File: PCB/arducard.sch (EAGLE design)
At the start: 94 parts, among them J1 USB MICRO, Q1 BC817-16LT1SMD, Q2 DMG2301U-7, Q3 2N7002, Q4 BSS84, Q5 2N7002, Q6 2N7002, Q7 2N7002, Q8 BSS84, Q9 DMG2301U-7, U1 microSD, U2 ATMEGA32U4-XUAU, Y1 8MHz KX-7

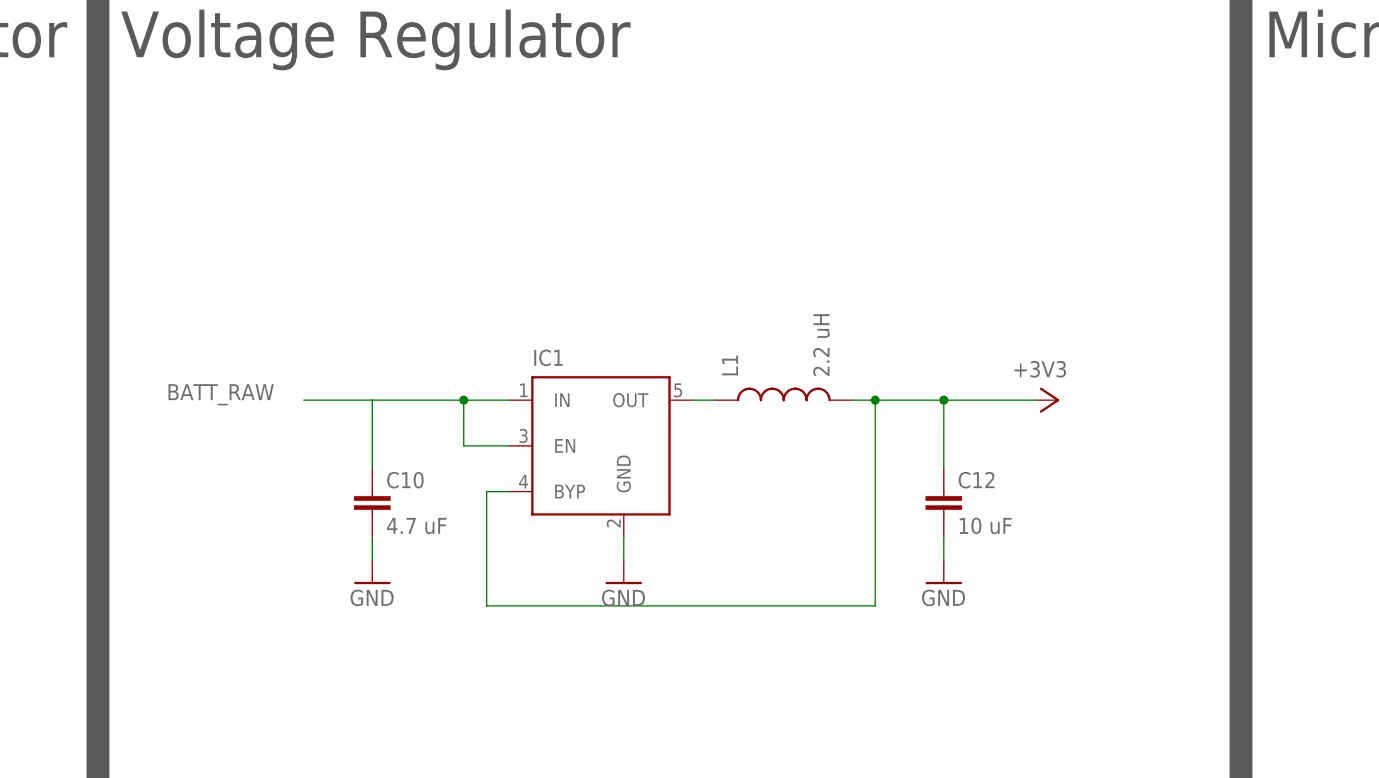
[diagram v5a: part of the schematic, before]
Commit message: added switch between Vusb and battery
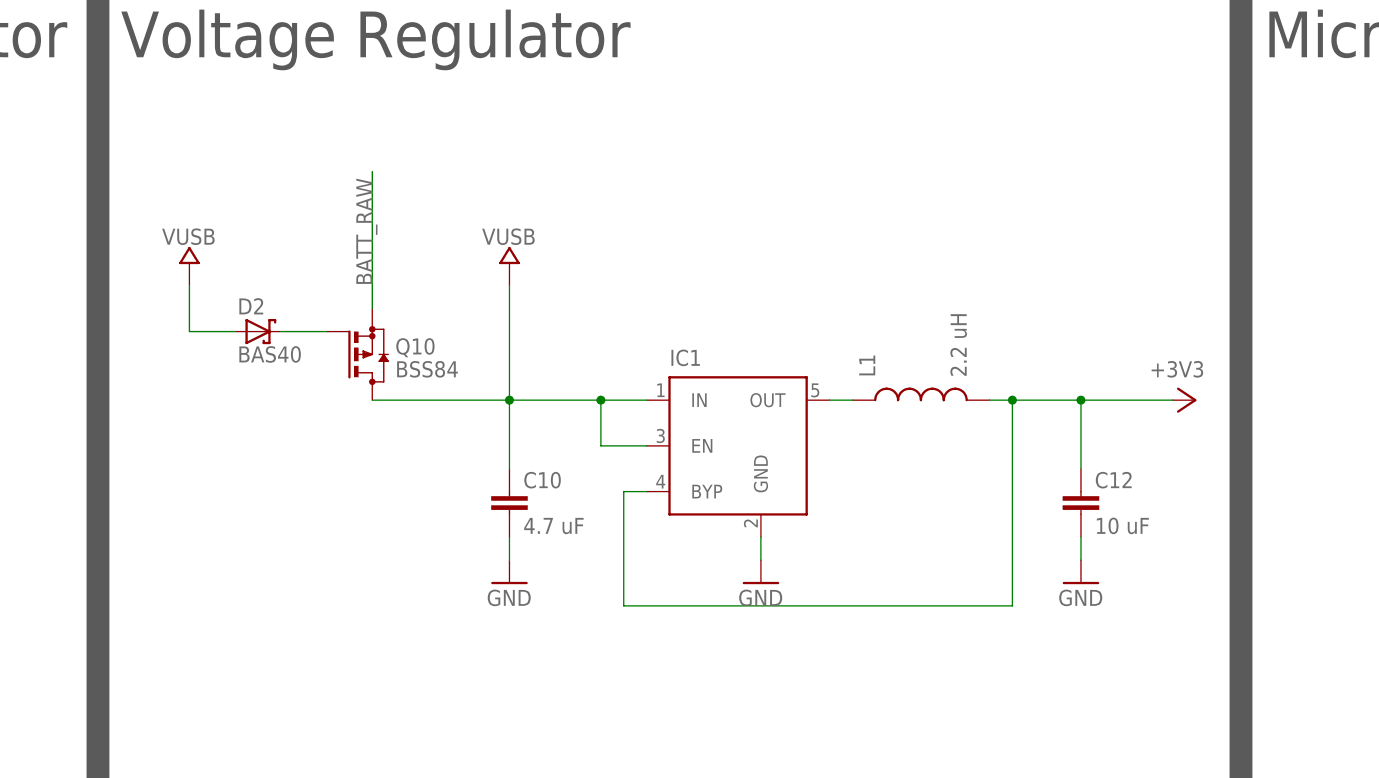
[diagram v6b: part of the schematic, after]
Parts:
- added D2: BAS40, diode:BAS40
- added Q10: BSS84, transistor-small-signal:BSS84
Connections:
- new net N$35: D2.C, Q10.G
- net BATT_RAW: now also Q10.S; no longer C10.1, IC1.EN, IC1.IN
- net VUSB: now also C10.1, D2.A, IC1.EN, IC1.IN, Q10.D
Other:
- moved on the sheet: C10, C12, IC1, L1
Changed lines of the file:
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@@
 <part name="+3V10" library="supply1" deviceset="+3V3" device=""/>
 <part name="GND31" library="supply1" deviceset="GND" device=""/>
+<part name="Q10" library="transistor-small-signal" deviceset="BSS84" device=""/>
+<part name="U$12" library="MyPOW" deviceset="VUSB" device=""/>
+<part name="D2" library="diode" deviceset="BAS40" device=""/>
+<part name="U$13" library="MyPOW" deviceset="VUSB" device=""/>
 </parts>
 <sheets>
@@
 <instance part="C5" gate="G$1" x="335.28" y="254"/>
 <instance part="+3V4" gate="G$1" x="45.72" y="142.24"/>
-<instance part="IC1" gate="G1" x="528.32" y="243.84"/>
-<instance part="L1" gate="G$1" x="548.64" y="248.92" rot="R90"/>
-<instance part="C12" gate="G$1" x="566.42" y="238.76"/>
-<instance part="+3V5" gate="G$1" x="579.12" y="248.92" rot="R270"/>
+<instance part="IC1" gate="G1" x="543.56" y="243.84"/>
+<instance part="L1" gate="G$1" x="563.88" y="248.92" rot="R90"/>
+<instance part="C12" gate="G$1" x="581.66" y="238.76"/>
+<instance part="+3V5" gate="G$1" x="594.36" y="248.92" rot="R270"/>
 <instance part="+3V6" gate="G$1" x="678.18" y="246.38" rot="R270"/>
 <instance part="U$8" gate="G$1" x="60.96" y="264.16"/>
@@
 <instance part="GND5" gate="1" x="127" y="228.6" rot="R270"/>
 <instance part="GND7" gate="1" x="642.62" y="218.44"/>
-<instance part="GND11" gate="1" x="530.86" y="228.6"/>
-<instance part="GND13" gate="1" x="566.42" y="228.6"/>
+<instance part="GND11" gate="1" x="546.1" y="228.6"/>
+<instance part="GND13" gate="1" x="581.66" y="228.6"/>
 <instance part="Q1" gate="G$1" x="406.4" y="86.36"/>
 <instance part="R15" gate="G$1" x="386.08" y="86.36" smashed="yes">
@@
 <instance part="+3V7" gate="G$1" x="299.72" y="254" rot="R270"/>
 <instance part="GND12" gate="1" x="238.76" y="223.52"/>
-<instance part="C10" gate="G$1" x="502.92" y="238.76"/>
-<instance part="GND17" gate="1" x="502.92" y="228.6"/>
+<instance part="C10" gate="G$1" x="518.16" y="238.76"/>
+<instance part="GND17" gate="1" x="518.16" y="228.6"/>
 <instance part="+3V8" gate="G$1" x="220.98" y="236.22" rot="R90"/>
 <instance part="+3V10" gate="G$1" x="241.3" y="269.24"/>
 <instance part="GND31" gate="1" x="292.1" y="233.68"/>
+<instance part="Q10" gate="G$1" x="502.92" y="254"/>
+<instance part="U$12" gate="G$1" x="518.16" y="264.16"/>
+<instance part="D2" gate="1" x="490.22" y="256.54"/>
+<instance part="U$13" gate="G$1" x="482.6" y="264.16"/>
 </instances>
 <busses>
@@
 <segment>
 <pinref part="IC1" gate="G1" pin="GND"/>
-<wire x1="530.86" y1="233.68" x2="530.86" y2="231.14" width="0.1524" layer="91"/>
+<wire x1="546.1" y1="233.68" x2="546.1" y2="231.14" width="0.1524" layer="91"/>
 <pinref part="GND11" gate="1" pin="GND"/>
 </segment>
 <segment>
 <pinref part="C12" gate="G$1" pin="2"/>
-<wire x1="566.42" y1="233.68" x2="566.42" y2="231.14" width="0.1524" layer="91"/>
+<wire x1="581.66" y1="233.68" x2="581.66" y2="231.14" width="0.1524" layer="91"/>
 <pinref part="GND13" gate="1" pin="GND"/>
 </segment>
@@
 <pinref part="GND17" gate="1" pin="GND"/>
 <pinref part="C10" gate="G$1" pin="2"/>
-<wire x1="502.92" y1="231.14" x2="502.92" y2="233.68" width="0.1524" layer="91"/>
+<wire x1="518.16" y1="231.14" x2="518.16" y2="233.68" width="0.1524" layer="91"/>
 </segment>
 <segment>
@@
 <junction x="335.28" y="256.54"/>
 <label x="325.12" y="256.54" size="1.778" layer="95"/>
+</segment>
+<segment>
+<pinref part="IC1" gate="G1" pin="IN"/>
+<wire x1="528.32" y1="248.92" x2="533.4" y2="248.92" width="0.1524" layer="91"/>
+<pinref part="IC1" gate="G1" pin="EN"/>
+<wire x1="533.4" y1="243.84" x2="528.32" y2="243.84" width="0.1524" layer="91"/>
+<wire x1="528.32" y1="243.84" x2="528.32" y2="248.92" width="0.1524" layer="91"/>
+<wire x1="528.32" y1="248.92" x2="518.16" y2="248.92" width="0.1524" layer="91"/>
+<junction x="528.32" y="248.92"/>
+<pinref part="C10" gate="G$1" pin="1"/>
+<wire x1="518.16" y1="241.3" x2="518.16" y2="248.92" width="0.1524" layer="91"/>
+<pinref part="Q10" gate="G$1" pin="D"/>
+<wire x1="502.92" y1="248.92" x2="518.16" y2="248.92" width="0.1524" layer="91"/>
+<junction x="518.16" y="248.92"/>
+<pinref part="U$12" gate="G$1" pin="VUSB"/>
+<wire x1="518.16" y1="248.92" x2="518.16" y2="261.62" width="0.1524" layer="91"/>
+</segment>
+<segment>
+<pinref part="U$13" gate="G$1" pin="VUSB"/>
+<wire x1="482.6" y1="261.62" x2="482.6" y2="256.54" width="0.1524" layer="91"/>
+<pinref part="D2" gate="1" pin="A"/>
+<wire x1="482.6" y1="256.54" x2="487.68" y2="256.54" width="0.1524" layer="91"/>
 </segment>
 </net>
@@
 </segment>
 <segment>
-<wire x1="556.26" y1="248.92" x2="558.8" y2="248.92" width="0.1524" layer="91"/>
+<wire x1="571.5" y1="248.92" x2="574.04" y2="248.92" width="0.1524" layer="91"/>
 <pinref part="L1" gate="G$1" pin="2"/>
 <pinref part="C12" gate="G$1" pin="1"/>
-<wire x1="558.8" y1="248.92" x2="566.42" y2="248.92" width="0.1524" layer="91"/>
-<wire x1="566.42" y1="248.92" x2="576.58" y2="248.92" width="0.1524" layer="91"/>
-<wire x1="566.42" y1="241.3" x2="566.42" y2="248.92" width="0.1524" layer="91"/>
-<junction x="566.42" y="248.92"/>
+<wire x1="574.04" y1="248.92" x2="581.66" y2="248.92" width="0.1524" layer="91"/>
+<wire x1="581.66" y1="248.92" x2="591.82" y2="248.92" width="0.1524" layer="91"/>
+<wire x1="581.66" y1="241.3" x2="581.66" y2="248.92" width="0.1524" layer="91"/>
+<junction x="581.66" y="248.92"/>
 <pinref part="+3V5" gate="G$1" pin="+3V3"/>
 <pinref part="IC1" gate="G1" pin="BYP"/>
-<wire x1="518.16" y1="238.76" x2="515.62" y2="238.76" width="0.1524" layer="91"/>
-<wire x1="515.62" y1="238.76" x2="515.62" y2="226.06" width="0.1524" layer="91"/>
-<wire x1="515.62" y1="226.06" x2="558.8" y2="226.06" width="0.1524" layer="91"/>
-<wire x1="558.8" y1="226.06" x2="558.8" y2="248.92" width="0.1524" layer="91"/>
-<junction x="558.8" y="248.92"/>
+<wire x1="533.4" y1="238.76" x2="530.86" y2="238.76" width="0.1524" layer="91"/>
+<wire x1="530.86" y1="238.76" x2="530.86" y2="226.06" width="0.1524" layer="91"/>
+<wire x1="530.86" y1="226.06" x2="574.04" y2="226.06" width="0.1524" layer="91"/>
+<wire x1="574.04" y1="226.06" x2="574.04" y2="248.92" width="0.1524" layer="91"/>
+<junction x="574.04" y="248.92"/>
 </segment>
 <segment>
@@
 <net name="BATT_RAW" class="0">
 <segment>
-<pinref part="IC1" gate="G1" pin="IN"/>
-<wire x1="513.08" y1="248.92" x2="518.16" y2="248.92" width="0.1524" layer="91"/>
-<pinref part="IC1" gate="G1" pin="EN"/>
-<wire x1="518.16" y1="243.84" x2="513.08" y2="243.84" width="0.1524" layer="91"/>
-<wire x1="513.08" y1="243.84" x2="513.08" y2="248.92" width="0.1524" layer="91"/>
-<wire x1="513.08" y1="248.92" x2="502.92" y2="248.92" width="0.1524" layer="91"/>
-<label x="480.06" y="248.92" size="1.778" layer="95"/>
-<junction x="513.08" y="248.92"/>
-<pinref part="C10" gate="G$1" pin="1"/>
-<wire x1="502.92" y1="248.92" x2="495.3" y2="248.92" width="0.1524" layer="91"/>
-<wire x1="502.92" y1="241.3" x2="502.92" y2="248.92" width="0.1524" layer="91"/>
-</segment>
-<segment>
 <pinref part="R16" gate="G$1" pin="2"/>
 <wire x1="408.94" y1="109.22" x2="419.1" y2="109.22" width="0.1524" layer="91"/>
@@
 <pinref part="U$6" gate="G$1" pin="+"/>
 </segment>
+<segment>
+<pinref part="Q10" gate="G$1" pin="S"/>
+<wire x1="502.92" y1="259.08" x2="502.92" y2="274.32" width="0.1524" layer="91"/>
+<label x="502.92" y="261.62" size="1.778" layer="95" rot="R90"/>
+</segment>
 </net>
 <net name="N$7" class="0">
@@
 <pinref part="IC1" gate="G1" pin="OUT"/>
 <pinref part="L1" gate="G$1" pin="1"/>
-<wire x1="538.48" y1="248.92" x2="541.02" y2="248.92" width="0.1524" layer="91"/>
+<wire x1="553.72" y1="248.92" x2="556.26" y2="248.92" width="0.1524" layer="91"/>
 </segment>
 </net>
@@
 </segment>
 </net>
+<net name="N$35" class="0">
+<segment>
+<pinref part="D2" gate="1" pin="C"/>
+<pinref part="Q10" gate="G$1" pin="G"/>
+<wire x1="492.76" y1="256.54" x2="497.84" y2="256.54" width="0.1524" layer="91"/>
+</segment>
+</net>

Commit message: fixed up libraries
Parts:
- removed IC1: (no value), v-reg-micrel:MIC5219XX
- added J2: microSD, SparkFun:USD-SOCKETSMD
- C11: value 1uF -> 10 uF
- C12: value 10 uF -> 100pF
- C13: value 100pF -> 22 pF
- C14: value 22 pF -> 1uF
- C6: value 100nF -> 1uF
- C7: value 1uF -> 100nF
- D1: value BAT54S -> BAS40; device diode:BAT54S -> diode:BAS40
- D2: value BAS40 -> BAT54S; device diode:BAS40 -> diode:BAT54S
- L1: value 2.2 uH -> MH2029-300Y; device SparkFun-Passives:INDUCTOR30OHM,1.8A -> wuerth-elektronik:WE-CBF_0805
- L2: value MH2029-300Y -> 2.2 uH; device wuerth-elektronik:WE-CBF_0805 -> SparkFun-Passives:INDUCTOR30OHM,1.8A
- Q1: value BC817-16LT1SMD -> BSS84; device transistor-npn:BC817-16LT1SMD -> transistor-small-signal:BSS84
- Q10: value BSS84 -> DMG2301U-7; device transistor-small-signal:BSS84 -> transistor-fet:DMG2301U-7
- Q2: value DMG2301U-7 -> BC817-16LT1SMD; device transistor-fet:DMG2301U-7 -> transistor-npn:BC817-16LT1SMD
- Q3: value 2N7002 -> DMG2301U-7; device AWJLEagleLib:2N7002 -> transistor-fet:DMG2301U-7
- Q4, Q8: value BSS84 -> 2N7002; device transistor-small-signal:BSS84 -> AWJLEagleLib:2N7002
- Q5: value 2N7002 -> BSS84; device AWJLEagleLib:2N7002 -> transistor-small-signal:BSS84
- Q9: value DMG2301U-7 -> BSS84; device transistor-fet:DMG2301U-7 -> transistor-small-signal:BSS84
- R11, R13, R9: value 150 -> 10k
- R14: value 22R -> 150
- R15: value 2k -> 150
- R16, R22: value 100k -> 150
- R17: value 39k -> 150
- R18: value 10k -> 150
- R20: value 2k -> 18.2k
- R21: value 18.2k -> 10k
- R23: value 100k -> 2k
- R25: value 33k -> 100k
- R26: value 150 -> 100k
- R27: value 10k -> 33k
- R3: value 10k -> 22R
- R5: value 150 -> 2k
- R6: value 10k -> 100k
- R7: value 150 -> 39k
- U1: value microSD -> ATMEGA32U4-XUAU; device SparkFun:USD-SOCKETSMD -> SmartPrj:ATMEGA32U4-XUAU
- U2: value ATMEGA32U4-XUAU -> (none); device SmartPrj:ATMEGA32U4-XUAU -> v-reg-micrel:MIC5219XX
- Y2: value SSP-T7-F -> 32.768 kHz
- renumbered U$1 to SW4, U$10 to U4, U$11 to SW2, U$14 to SW3, U$2 to J3, U$3 to U5, U$4 to B1, U$5 to U3, U$6 to B2, U$7 to Y2, U$8 to SW0, U$9 to SW1
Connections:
- removed net N$10: Q1.B, R15.2
- new net Q2: Q2.B, R5.2
- net +3V3: now also C13.1, C5.1, J2.VCC, L2.2, Q10.S, R21.2, U1.AVCC, U1.AVCC1, U1.UVCC, U1.VCC1, U2.BYP; no longer C12.1, C14.1, IC1.BYP, L1.2, Q8.S, R3.2, U2.AVCC, U2.AVCC1, U2.UVCC, U2.VCC, U2.VCC1
- net B0: now also R14.1, U1.(OC0B/SCL/INT0)PD0; no longer R5.1, U2.(OC0B/SCL/INT0)PD0
- net B1: now also R15.1, U1.(SDA/INT1)PD1; no longer R7.1, U2.(SDA/INT1)PD1
- net B2: now also R16.1, U1.(RXD1/AIN1/INT2)PD2; no longer R9.1, U2.(RXD1/AIN1/INT2)PD2
- net B3: now also R17.1, U1.(TXD1/INT3)PD3; no longer R11.1, U2.(TXD1/INT3)PD3
- net B4: now also R18.1, U1.(ADC11/PCINT4)PB4; no longer R26.1, U2.(ADC11/PCINT4)PB4
- net BATTSENS: now also R7.1, R8.2, U1.(ADC1)PF1; no longer R17.1, R18.2, U2.(ADC1)PF1
- net BATTSENS_EN: now also R5.1, U1.(ADC0)PF0; no longer R15.1, U2.(ADC0)PF0
- net BATT_RAW: now also C12.1, Q1.S, Q3.S, R6.2; no longer C13.1, Q10.S, Q2.S, R16.2
- net BORDER: now also Q4.D, R24.2; no longer Q3.D, R22.2
- net BORDER_CONTROL: now also Q5.G, U1.(ADC7/TDI)PF7; no longer Q4.G, U2.(ADC7/TDI)PF7
- net CDP: now also J2.CD1, J2.CD2, R21.1, R22.1; no longer R13.1, R2.1, U1.CD1, U1.CD2
- net CHGSTAT: now also U1.(SS/PCINT0)PB0; no longer U2.(SS/PCINT0)PB0
- net D+: now also R3.1; no longer R4.1
- net D-: now also R4.1; no longer R14.1
- net DISCHARGE: now also Q7.G, U1.(ADC5/TMS)PF5; no longer Q5.G, U2.(ADC5/TMS)PF5
- net EPD_CS: now also U1.(T0/OC4D/ADC10)PD7; no longer U2.(T0/OC4D/ADC10)PD7
- net FRAM_CS: now also U1.(ICP1/ADC8)PD4; no longer U2.(ICP1/ADC8)PD4
- net GND: now also C13.2, D2.C2, J2.GND, J2.SHIELD1, J2.SHIELD2, L1.1, L1.2, Q2.E, Q8.S, R11.2, R13.2, R20.1, R8.1, R9.2, U1.GND1, U1.GND2, U1.GND3, U1.PAD, U1.UGND; no longer C12.2, D1.C2, IC1.GND, L2.1, L2.2, Q1.E, Q5.S, R18.1, R21.1, R27.2, R6.2, R8.2, U1.SHIELD1, U1.SHIELD2, U2.GND1, U2.GND2, U2.GND3, U2.PAD, U2.UGND
- net MISO: now also J2.DO, U1.(PD0/MISO/PCINT3)PB3; no longer U1.DO, U2.(PD0/MISO/PCINT3)PB3
- net MOSI: now also J2.DI, U1.(PDI/MOSI/PCINT2)PB2; no longer U1.DI, U2.(PDI/MOSI/PCINT2)PB2
- net N$11: now also C12.2, Q2.C, Q3.G, R6.1; no longer C13.2, Q1.C, Q2.G, R16.1
- net N$13: now also Q3.D, R7.2; no longer Q2.D, R17.2
- net N$2: now also R10.1, R15.2; no longer R7.2, R8.1
- net N$3: now also R14.2, R9.1; no longer R5.2, R6.1
- net N$34: now also Q8.D, R27.1; no longer Q7.D, R25.1
- net N$35: now also D1.C, Q1.G; no longer D2.C, Q10.G
- net N$37: now also R20.2; no longer R21.2
- net N$38: now also Q5.D, R26.2; no longer Q4.D, R24.2
- net N$39: now also Q4.G, R25.2, R26.1; no longer Q3.G, R23.2, R24.1
- net N$40: now also D2.C1A2; no longer D1.C1A2
- net N$44: now also Q10.G, Q9.D, R27.2; no longer Q8.D, Q9.G, R25.2
- net N$5: now also R11.1, R16.2; no longer R10.1, R9.2
- net N$6: now also R17.2; no longer R11.2
- net N$7: now also L2.1, U2.OUT; no longer IC1.OUT, L1.1
- net N$8: now also R13.1, R18.2; no longer R26.2, R27.1
- net N$9: now also C7.1, U1.AREF; no longer C6.1, U2.AREF
- net PANEL_ON: now also Q9.G, U1.(ADC6/TDO)PF6; no longer Q7.G, U2.(ADC6/TDO)PF6
- net PWM: now also U1.(PCINT7/OC0A/OC1C/#RTS)PB7; no longer U2.(PCINT7/OC0A/OC1C/#RTS)PB7
- net RD+: now also R3.2, U1.D+; no longer R4.2, U2.D+
- net RD-: now also R4.2, U1.D-; no longer R14.2, U2.D-
- net RESET: now also R2.1, U1.RESET; no longer R3.1, U2.RESET
- net RTC_CS: now also U1.(T1/#OC4D/ADC9)PD6; no longer U2.(T1/#OC4D/ADC9)PD6
- net RTC_INT: now also U1.(PCINT6/OC1B/OC4B/ADC13)PB6; no longer U2.(PCINT6/OC1B/OC4B/ADC13)PB6
- net SCK: now also J2.SCK, U1.(SCLK/PCINT1)PB1; no longer U1.SCK, U2.(SCLK/PCINT1)PB1
- net SD_CD: now also R22.2, U1.(PCINT5/OC1A/#OC4B/ADC12)PB5; no longer R13.2, U2.(PCINT5/OC1A/#OC4B/ADC12)PB5
- net SD_CS: now also J2.CS, U1.(XCK1/#CTS)PD5; no longer U1.CS, U2.(XCK1/#CTS)PD5
- net UCAP: now also C6.1, U1.UCAP; no longer C7.1, U2.UCAP
- net VCC_T: now also Q10.D, Q5.S; no longer Q4.S, Q9.D
- net VCOM: now also R23.1, R24.1; no longer R20.1, R22.1
- net VCOM_DRIVER: now also R23.2; no longer R20.2
- net VDH: now also Q7.D; no longer Q6.D
- net VDL: now also Q4.S, R25.1; no longer Q3.S, R23.1
- net VGH: now also Q6.D; no longer Q5.D
- net VGL: now also D2.A1; no longer D1.A1
- net VUSB: now also C14.1, D1.A, Q1.D, U1.VBUS, U2.EN, U2.IN; no longer C5.1, D2.A, IC1.EN, IC1.IN, Q10.D, U2.VBUS
- net XTAL1: now also U1.XTAL1; no longer U2.XTAL1
- net XTAL2: now also U1.XTAL2; no longer U2.XTAL2
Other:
- moved on the sheet: C11, C12, C13, C14, C5, C6, C7, Q3, Q6, Q7, R10, R11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

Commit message: initial board layout
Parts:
- added R28: 10k, SmartPrj:R-EU_R0603
- renumbered JP1 to J4
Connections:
- removed net N$35: D1.C, Q1.G
- new net N$10: D1.C
- net BATT_RAW: now also Q1.D; no longer Q1.S
- net CDP: no longer J2.CD1
- net GND: now also R28.1
- net VUSB: now also Q1.G, Q1.S, R28.2; no longer Q1.D
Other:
- note added: "MicroUSB Connector"
- note removed: "USB Micro Connector"
- moved on the sheet: D1, Q1
